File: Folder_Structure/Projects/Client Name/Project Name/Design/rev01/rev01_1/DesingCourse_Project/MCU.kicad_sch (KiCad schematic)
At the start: 43 parts, among them J3 874380243, J4 874380843, J5 874380343, J6 874380643, U3 STM32F405RGTx, Y1 8MHz

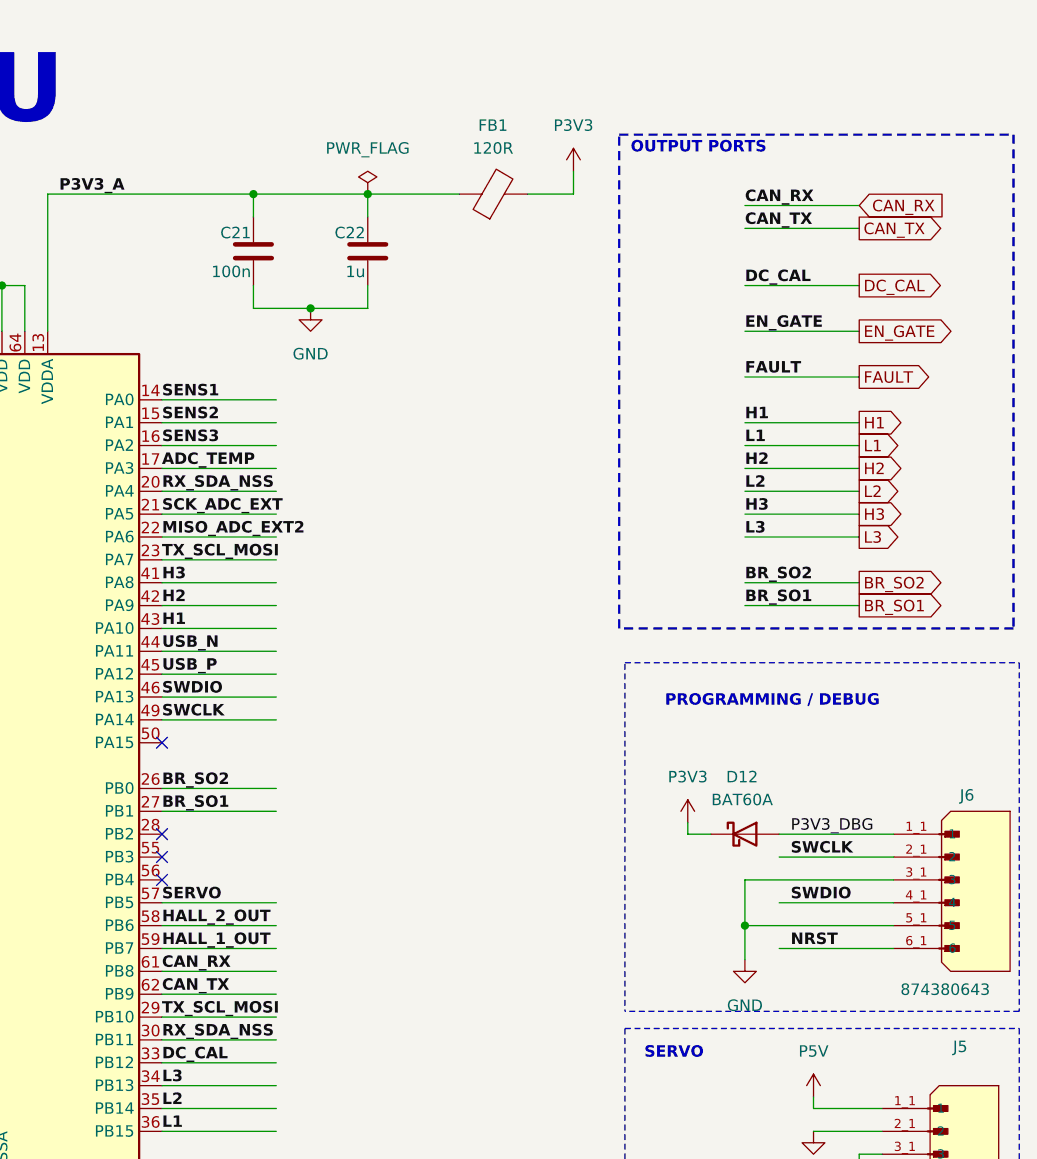
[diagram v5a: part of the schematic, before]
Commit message: Update19
PCB finished before applying curved traces
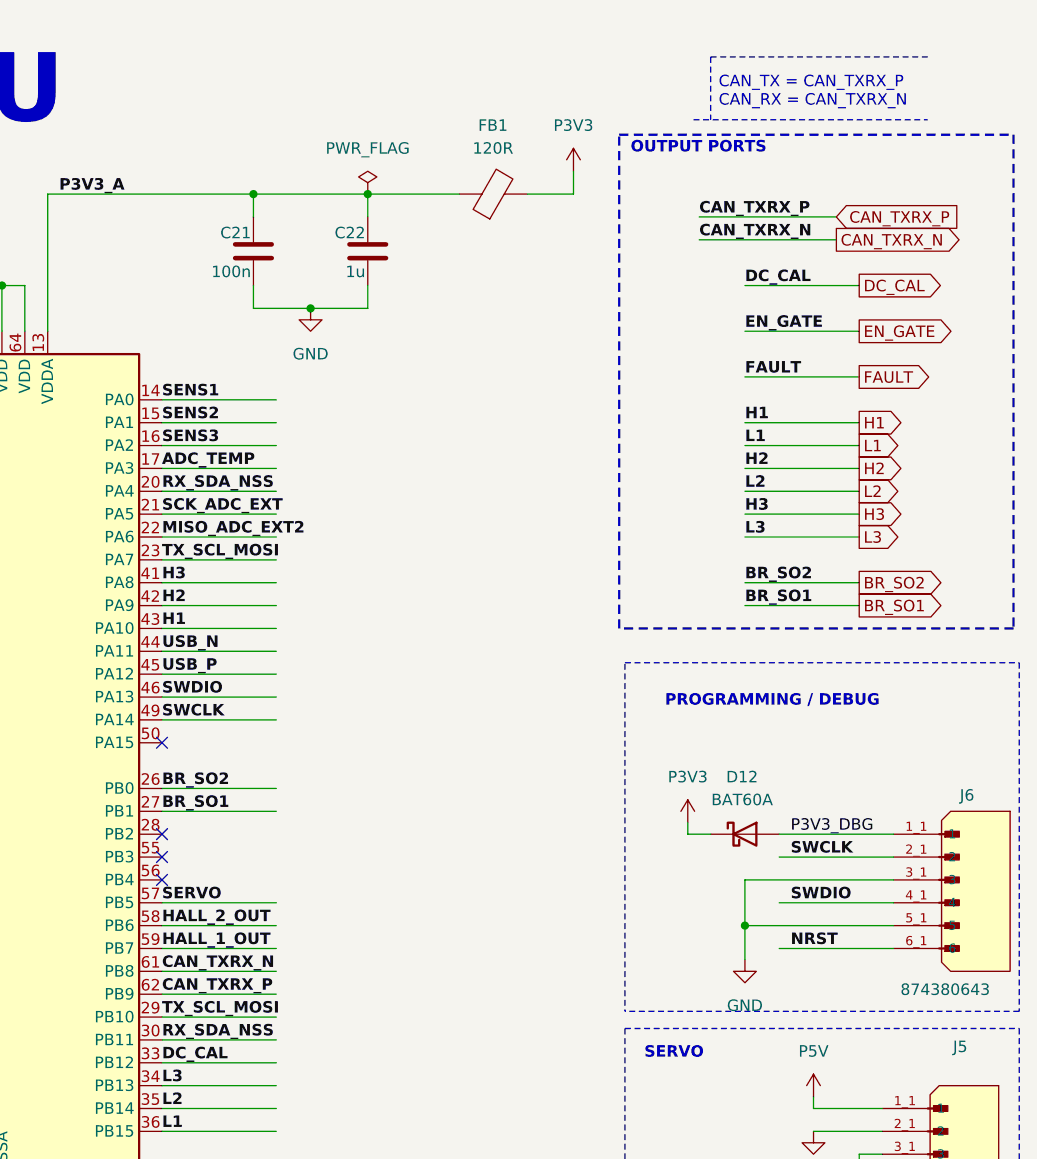
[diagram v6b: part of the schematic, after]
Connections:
- net CAN_RX renamed CAN_TXRX_N
- net CAN_TX renamed CAN_TXRX_P
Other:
- note added: "CAN_TX = CAN_TXRX_P CAN_RX = CAN_TXRX_N"
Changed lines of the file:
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@@
 		)
 	)
+	(text "CAN_TX = CAN_TXRX_P\nCAN_RX = CAN_TXRX_N\n"
+		(exclude_from_sim no)
+		(at 245.999 20.447 0)
+		(effects
+			(font
+				(size 1.27 1.27)
+			)
+			(justify left)
+		)
+	)
 	(text "WHEN:\nVDC = 60V =>\nAN_IN = 3V204"
 		(exclude_from_sim no)
@@
 	(wire
 		(pts
-			(xy 248.92 35.56) (xy 261.62 35.56)
-		)
-		(stroke
-			(width 0)
-			(type default)
-		)
-	)
-	(wire
-		(pts
 			(xy 88.9 171.45) (xy 88.9 177.8)
 		)
@@
 		)
 	)
+	(polyline
+		(pts
+			(xy 245.11 16.51) (xy 245.11 23.495)
+		)
+		(stroke
+			(width 0)
+			(type dash)
+		)
+	)
 	(wire
 		(pts
@@
 	(wire
 		(pts
+			(xy 243.84 34.29) (xy 259.08 34.29)
+		)
+		(stroke
+			(width 0)
+			(type default)
+		)
+	)
+	(wire
+		(pts
 			(xy 30.48 39.37) (xy 44.45 39.37)
 		)
@@
 		)
 	)
+	(polyline
+		(pts
+			(xy 269.24 16.51) (xy 245.11 16.51)
+		)
+		(stroke
+			(width 0)
+			(type dash)
+		)
+	)
 	(wire
 		(pts
@@
 	(wire
 		(pts
-			(xy 248.92 33.02) (xy 261.62 33.02)
+			(xy 29.21 186.69) (xy 57.15 186.69)
 		)
 		(stroke
@@
 	(wire
 		(pts
-			(xy 29.21 186.69) (xy 57.15 186.69)
+			(xy 243.84 36.83) (xy 259.08 36.83)
 		)
 		(stroke
@@
 		)
 	)
+	(polyline
+		(pts
+			(xy 243.205 23.495) (xy 269.24 23.495)
+		)
+		(stroke
+			(width 0)
+			(type dash)
+		)
+	)
 	(wire
 		(pts
@@
 		)
 	)
+	(label "CAN_TXRX_P"
+		(at 184.15 120.65 0)
+		(effects
+			(font
+				(size 1.27 1.27)
+				(thickness 0.254)
+				(bold yes)
+			)
+			(justify left bottom)
+		)
+	)
 	(label "P5V_COM"
 		(at 41.91 171.45 0)
@@
 		)
 	)
-	(label "CAN_TX"
-		(at 184.15 120.65 0)
+	(label "USB_N"
+		(at 38.1 62.23 0)
 		(effects
 			(font
 				(size 1.27 1.27)
-				(thickness 0.254)
-				(bold yes)
 			)
 			(justify left bottom)
 		)
 	)
-	(label "USB_N"
-		(at 38.1 62.23 0)
+	(label "CAN_TXRX_P"
+		(at 243.84 34.29 0)
 		(effects
 			(font
 				(size 1.27 1.27)
+				(thickness 0.254)
+				(bold yes)
 			)
 			(justify left bottom)
@@
 		)
 	)
-	(label "CAN_TX"
-		(at 248.92 35.56 0)
-		(effects
-			(font
-				(size 1.27 1.27)
-				(thickness 0.254)
-				(bold yes)
-			)
-			(justify left bottom)
-		)
-	)
 	(label "PH1_P"
 		(at 134.62 67.31 0)
@@
 		)
 	)
+	(label "CAN_TXRX_N"
+		(at 243.84 36.83 0)
+		(effects
+			(font
+				(size 1.27 1.27)
+				(thickness 0.254)
+				(bold yes)
+			)
+			(justify left bottom)
+		)
+	)
 	(label "DC_CAL"
 		(at 248.92 41.91 0)
@@
 		)
 	)
-	(label "H2"
-		(at 248.92 62.23 0)
+	(label "CAN_TXRX_N"
+		(at 184.15 118.11 0)
 		(effects
 			(font
@@
 		)
 	)
-	(label "SERVO"
-		(at 242.57 147.32 0)
+	(label "H2"
+		(at 248.92 62.23 0)
 		(effects
 			(font
@@
 		)
 	)
-	(label "FAULT"
-		(at 130.81 107.95 0)
+	(label "SERVO"
+		(at 242.57 147.32 0)
 		(effects
 			(font
@@
 		)
 	)
-	(label "CAN_RX"
-		(at 184.15 118.11 0)
+	(label "FAULT"
+		(at 130.81 107.95 0)
 		(effects
 			(font
@@
 		)
 	)
-	(label "CAN_RX"
-		(at 248.92 33.02 0)
-		(effects
-			(font
-				(size 1.27 1.27)
-				(thickness 0.254)
-				(bold yes)
-			)
-			(justify left bottom)
-		)
-	)
 	(label "SENS2"
 		(at 30.48 50.8 0)
@@
 		)
 	)
-	(global_label "USB_P"
-		(shape bidirectional)
-		(at 35.56 64.77 180)
+	(global_label "CAN_TXRX_N"
+		(shape output)
+		(at 259.08 36.83 0)
 		(fields_autoplaced yes)
 		(effects
 			(font
 				(size 1.27 1.27)
+				(thickness 0.1588)
 			)
-			(justify right)
+			(justify left)
 		)
 		(property "Intersheetrefs" "${INTERSHEET_REFS}"
-			(at 25.4161 64.77 0)
+			(at 273.7717 36.83 0)
 			(effects
 				(font
 					(size 1.27 1.27)
 				)
-				(justify right)
+				(justify left)
 				(hide yes)
 			)
 		)
 	)
-	(global_label "L1"
-		(shape output)
-		(at 261.62 59.69 0)
+	(global_label "USB_P"
+		(shape bidirectional)
+		(at 35.56 64.77 180)
 		(fields_autoplaced yes)
 		(effects
@@
 				(size 1.27 1.27)
 			)
-			(justify left)
+			(justify right)
 		)
 		(property "Intersheetrefs" "${INTERSHEET_REFS}"
-			(at 266.9379 59.69 0)
+			(at 25.4161 64.77 0)
 			(effects
 				(font
 					(size 1.27 1.27)
 				)
-				(justify left)
+				(justify right)
 				(hide yes)
 			)
 		)
 	)
-	(global_label "CAN_TX"
+	(global_label "L1"
 		(shape output)
-		(at 261.62 35.56 0)
+		(at 261.62 59.69 0)
 		(fields_autoplaced yes)
 		(effects
 			(font
 				(size 1.27 1.27)
-				(thickness 0.1588)
 			)
 			(justify left)
 		)
 		(property "Intersheetrefs" "${INTERSHEET_REFS}"
-			(at 271.5341 35.56 0)
+			(at 266.9379 59.69 0)
 			(effects
 				(font
@@
 		)
 	)
-	(global_label "CAN_RX"
+	(global_label "HALL_3_OUT"
 		(shape input)
-		(at 261.62 33.02 0)
+		(at 30.48 31.75 180)
 		(fields_autoplaced yes)
 		(effects
 			(font
 				(size 1.27 1.27)
-				(thickness 0.1588)
 			)
-			(justify left)
+			(justify right)
 		)
 		(property "Intersheetrefs" "${INTERSHEET_REFS}"
-			(at 271.8365 33.02 0)
+			(at 16.1511 31.75 0)
 			(effects
 				(font
 					(size 1.27 1.27)
 				)
-				(justify left)
+				(justify right)
 				(hide yes)
 			)
 		)
 	)
-	(global_label "HALL_3_OUT"
+	(global_label "CAN_TXRX_P"
 		(shape input)
-		(at 30.48 31.75 180)
+		(at 259.08 34.29 0)
 		(fields_autoplaced yes)
 		(effects
 			(font
 				(size 1.27 1.27)
+				(thickness 0.1588)
 			)
-			(justify right)
+			(justify left)
 		)
 		(property "Intersheetrefs" "${INTERSHEET_REFS}"
-			(at 16.1511 31.75 0)
+			(at 273.7112 34.29 0)
 			(effects
 				(font
 					(size 1.27 1.27)
 				)
-				(justify right)
+				(justify left)
 				(hide yes)
 			)
